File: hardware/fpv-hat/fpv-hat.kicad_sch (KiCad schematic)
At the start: 0 parts

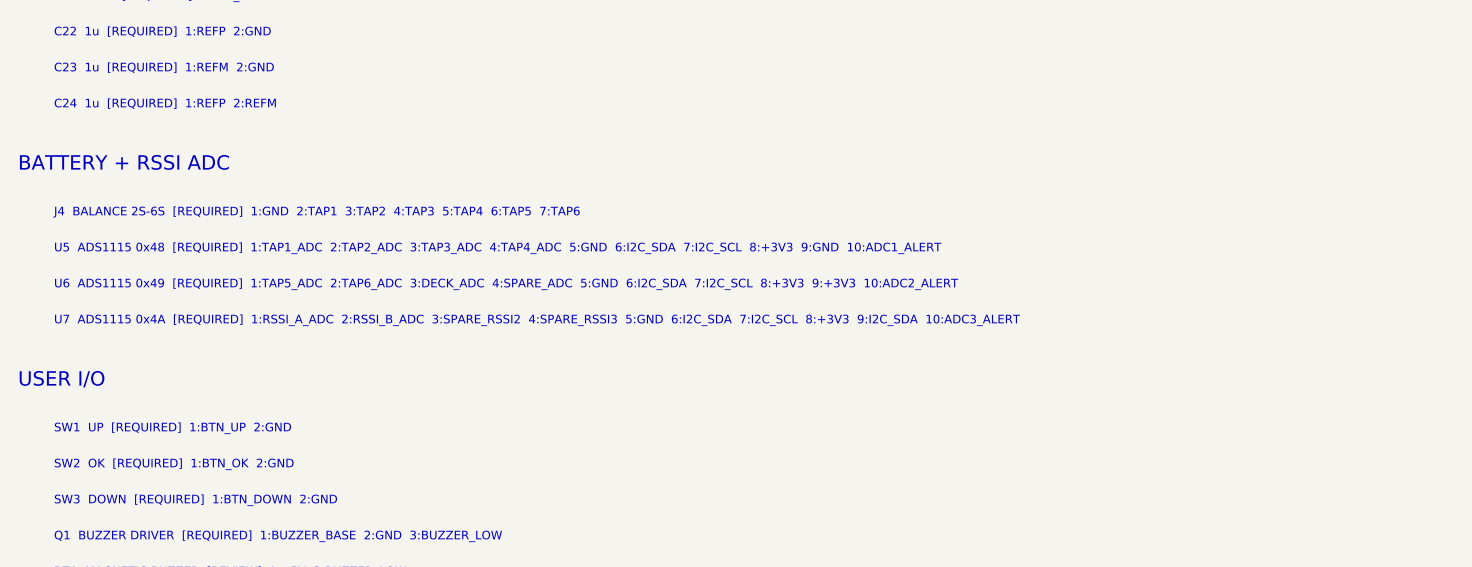
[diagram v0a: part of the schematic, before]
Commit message: fix(hw): correct ADS1115 pinout and decoupling
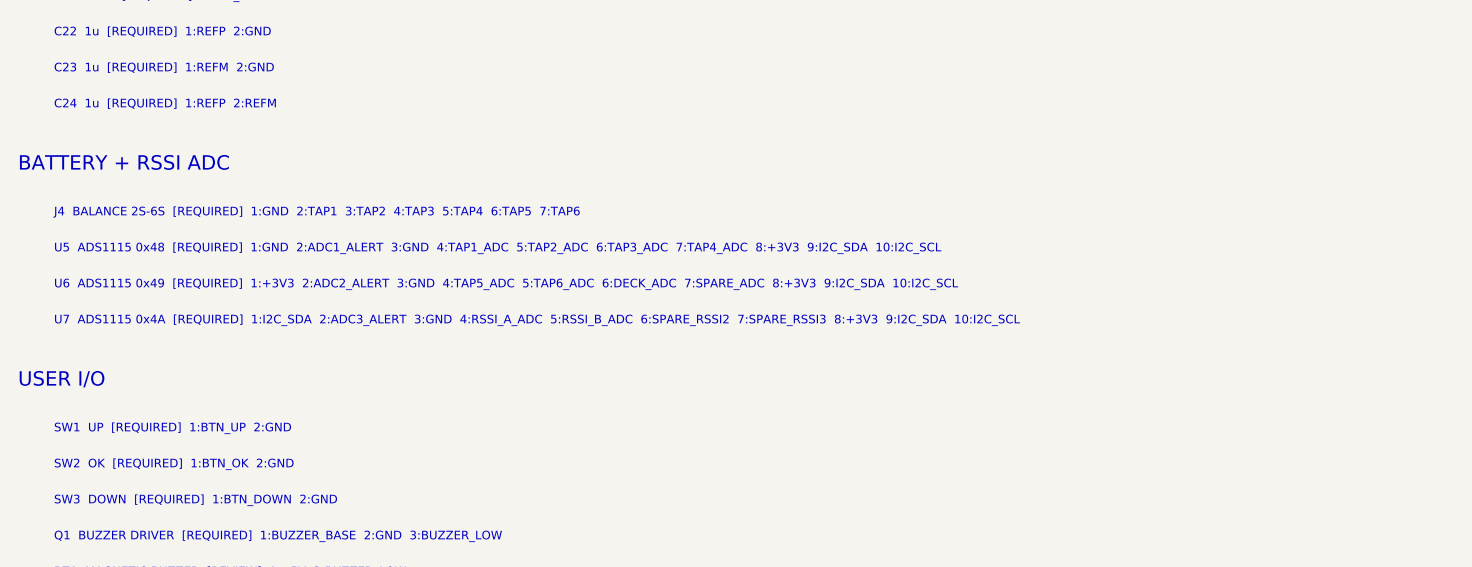
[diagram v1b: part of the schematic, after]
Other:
- note added: "U5 ADS1115 0x48 [REQUIRED] 1:GND 2:ADC1_ALERT 3:GND 4:TAP1_ADC 5:TAP2_ADC 6:TAP3_ADC 7:TAP4_ADC 8:+3V3 9:I2C_SDA 10:I2C_SCL"
- note added: "U6 ADS1115 0x49 [REQUIRED] 1:+3V3 2:ADC2_ALERT 3:GND 4:TAP5_ADC 5:TAP6_ADC 6:DECK_ADC 7:SPARE_ADC 8:+3V3 9:I2C_SDA 10:I2C_SCL"
- note added: "U7 ADS1115 0x4A [REQUIRED] 1:I2C_SDA 2:ADC3_ALERT 3:GND 4:RSSI_A_ADC 5:RSSI_B_ADC 6:SPARE_RSSI2 7:SPARE_RSSI3 8:+3V3 9:I2C_SDA 10:I2C_SCL"
- note removed: "U5 ADS1115 0x48 [REQUIRED] 1:TAP1_ADC 2:TAP2_ADC 3:TAP3_ADC 4:TAP4_ADC 5:GND 6:I2C_SDA 7:I2C_SCL 8:+3V3 9:GND 10:ADC1_ALERT"
- note removed: "U6 ADS1115 0x49 [REQUIRED] 1:TAP5_ADC 2:TAP6_ADC 3:DECK_ADC 4:SPARE_ADC 5:GND 6:I2C_SDA 7:I2C_SCL 8:+3V3 9:+3V3 10:ADC2_ALERT"
- note removed: "U7 ADS1115 0x4A [REQUIRED] 1:RSSI_A_ADC 2:RSSI_B_ADC 3:SPARE_RSSI2 4:SPARE_RSSI3 5:GND 6:I2C_SDA 7:I2C_SCL 8:+3V3 9:I2C_SDA 10:ADC3_ALERT"
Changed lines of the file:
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@@
     (effects (font (size 0.95 0.95)) (justify left bottom))
 )
-  (text "U5  ADS1115 0x48  [REQUIRED]  1:TAP1_ADC  2:TAP2_ADC  3:TAP3_ADC  4:TAP4_ADC  5:GND  6:I2C_SDA  7:I2C_SCL  8:+3V3  9:GND  10:ADC1_ALERT" (at 24 141 0)
+  (text "U5  ADS1115 0x48  [REQUIRED]  1:GND  2:ADC1_ALERT  3:GND  4:TAP1_ADC  5:TAP2_ADC  6:TAP3_ADC  7:TAP4_ADC  8:+3V3  9:I2C_SDA  10:I2C_SCL" (at 24 141 0)
     (effects (font (size 0.95 0.95)) (justify left bottom))
 )
-  (text "U6  ADS1115 0x49  [REQUIRED]  1:TAP5_ADC  2:TAP6_ADC  3:DECK_ADC  4:SPARE_ADC  5:GND  6:I2C_SDA  7:I2C_SCL  8:+3V3  9:+3V3  10:ADC2_ALERT" (at 24 145 0)
+  (text "U6  ADS1115 0x49  [REQUIRED]  1:+3V3  2:ADC2_ALERT  3:GND  4:TAP5_ADC  5:TAP6_ADC  6:DECK_ADC  7:SPARE_ADC  8:+3V3  9:I2C_SDA  10:I2C_SCL" (at 24 145 0)
     (effects (font (size 0.95 0.95)) (justify left bottom))
 )
-  (text "U7  ADS1115 0x4A  [REQUIRED]  1:RSSI_A_ADC  2:RSSI_B_ADC  3:SPARE_RSSI2  4:SPARE_RSSI3  5:GND  6:I2C_SDA  7:I2C_SCL  8:+3V3  9:I2C_SDA  10:ADC3_ALERT" (at 24 149 0)
+  (text "U7  ADS1115 0x4A  [REQUIRED]  1:I2C_SDA  2:ADC3_ALERT  3:GND  4:RSSI_A_ADC  5:RSSI_B_ADC  6:SPARE_RSSI2  7:SPARE_RSSI3  8:+3V3  9:I2C_SDA  10:I2C_SCL" (at 24 149 0)
     (effects (font (size 0.95 0.95)) (justify left bottom))
 )

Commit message: fix(hw): add verified decoder power networks
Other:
- note added: "CA1 100n 16V X7R [REQUIRED] 1:+3V3 2:GND"
- note added: "CA2 100n 16V X7R [REQUIRED] 1:+3V3 2:GND"
- note added: "CA3 100n 16V X7R [REQUIRED] 1:+3V3 2:GND"
- note added: "CD1 100n 16V X7R [REQUIRED] 1:+1V8A 2:GND"
- note added: "CD2 100n 16V X7R [REQUIRED] 1:+1V8A 2:GND"
- note added: "CD3 100n 16V X7R [REQUIRED] 1:+1V8D 2:GND"
- note added: "CD4 100n 16V X7R [REQUIRED] 1:+3V3 2:GND"
- note added: "CIN1 1u 10V X7R [REQUIRED] 1:+5V 2:GND"
- note added: "COUT1 1u 10V X7R [REQUIRED] 1:+1V8 2:GND"
- note added: "CY1 CRYSTAL LOAD TUNE [DNP] 1:XTAL1 2:GND"
- note added: "CY2 CRYSTAL LOAD TUNE [DNP] 1:XTAL2 2:GND"
- note added: "RY1 100k 1% [REQUIRED] 1:XTAL1 2:XTAL2"

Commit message: feat(hw): add dual RX5808 final-form HAT layout
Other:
- note added: "C1 100n 16V X7R [REQUIRED] 1:+3V3 2:GND"
- note added: "C2 100n 16V X7R [REQUIRED] 1:+3V3 2:GND"
- note added: "CRA1 100n 16V X7R [REQUIRED] 1:+5V_RX_A 2:GND"
- note added: "CRA2 10u 10V X7R [REQUIRED] 1:+5V_RX_A 2:GND"
- note added: "CRB1 100n 16V X7R [REQUIRED] 1:+5V_RX_B 2:GND"
- note added: "CRB2 10u 10V X7R [REQUIRED] 1:+5V_RX_B 2:GND"
- note added: "FRA 220R@100MHz 2A [REQUIRED] 1:+5V 2:+5V_RX_A"
- note added: "FRB 220R@100MHz 2A [REQUIRED] 1:+5V 2:+5V_RX_B"
- note added: "J1 WAVESHARE 40PIN [REQUIRED] 1:+5V 2:+3V3 3:+5V 4:I2C_SDA 5:GND 6:I2C_SCL 7:DVP_D0 8:VIDEO_SELECT_MCU 9:DVP_D1 11:DVP_D2 12:DVP_D3 14:DVP_D4 15:DVP_D5 16:DVP_D6 17:DVP_D7 18:+3V3 20:DVP_PCLK 22:DVP_HSYNC 24:DVP_VSYNC 26:GND 28:RX_DATA 30:RX_CLK 31:RX_LE_A 32:RX_LE_B 34:VIDEO_SELECT 35:TVP_RESETB 36:BTN_UP 37:BTN_OK 38:BTN_DOWN 39:BUZZER 40:GND"
- note added: "J3 SMA EDGE B [REQUIRED] 1:RF_B 2:GND"
- note added: "JP1 AUTO / MCU SELECT [REQUIRED] 1:RX_A_STRONGER 2:VIDEO_SELECT 3:VIDEO_SELECT_MCU"
- note added: "RXA RX5808 MODULE A [REQUIRED] 1:GND 2:RF_A 3:GND 4:RX_DATA 5:RX_LE_A 6:RX_CLK 7:GND 8:+5V_RX_A 9:RSSI_A 10:NC_AUDIO_A 11:VIDEO_A 12:GND"
- note added: "RXB RX5808 MODULE B [REQUIRED] 1:GND 2:RF_B 3:GND 4:RX_DATA 5:RX_LE_B 6:RX_CLK 7:GND 8:+5V_RX_B 9:RSSI_B 10:NC_AUDIO_B 11:VIDEO_B 12:GND"
- note added: "U1 RSSI COMPARATOR [REQUIRED] 1:RX_A_STRONGER 2:GND 3:RSSI_A_HYS 4:RSSI_B 5:+3V3"
- note added: "U2 VIDEO SWITCH [REQUIRED] 1:VIDEO_A 2:GND 3:VIDEO_B 4:VIDEO_SELECTED 5:+3V3 6:VIDEO_SELECT"
- note removed: "J1 WAVESHARE 40PIN [REQUIRED] 1:+5V 2:+3V3 3:+5V 4:I2C_SDA 5:GND 6:I2C_SCL 7:DVP_D0 9:DVP_D1 11:DVP_D2 12:DVP_D3 14:DVP_D4 15:DVP_D5 16:DVP_D6 17:DVP_D7 18:+3V3 20:DVP_PCLK 22:DVP_HSYNC 24:DVP_VSYNC 26:GND 28:RX_DATA 30:RX_CLK 31:RX_LE_A 32:RX_LE_B 34:ACTIVE_RX 35:TVP_RESETB 36:BTN_UP 37:BTN_OK 38:BTN_DOWN 39:BUZZER 40:GND"
- note removed: "J3 SMA EDGE B [DNP] 1:RF_B 2:GND"
- note removed: "RXA RX5808 MODULE A [REQUIRED] 1:GND 2:RF_A 3:GND 4:RX_DATA 5:RX_LE_A 6:RX_CLK 7:GND 8:+5V 9:RSSI_A 10:NC_AUDIO_A 11:VIDEO_A"
- note removed: "RXB RX5808 MODULE B [DNP] 1:GND 2:RF_B 3:GND 4:RX_DATA 5:RX_LE_B 6:RX_CLK 7:GND 8:+5V 9:RSSI_B 10:NC_AUDIO_B 11:VIDEO_B"
- note removed: "U1 RSSI COMPARATOR [REQUIRED] 1:ACTIVE_RX 2:GND 3:RSSI_A_HYS 4:RSSI_B 5:+3V3"
- note removed: "U2 VIDEO SWITCH [REQUIRED] 1:VIDEO_A 2:GND 3:VIDEO_B 4:VIDEO_SELECTED 5:+3V3 6:ACTIVE_RX"

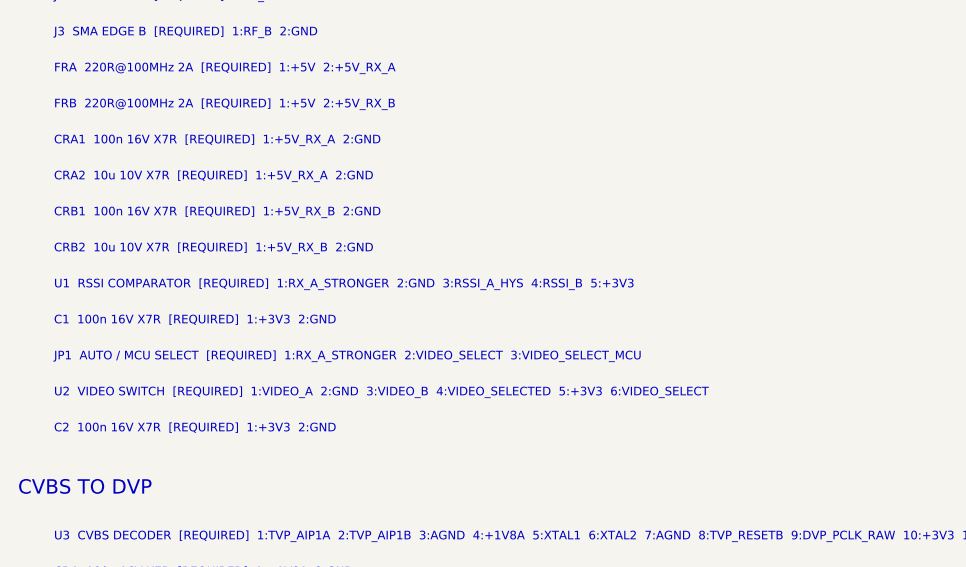
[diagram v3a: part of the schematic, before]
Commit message: fix(hw): correct LMV331 diversity pin mapping
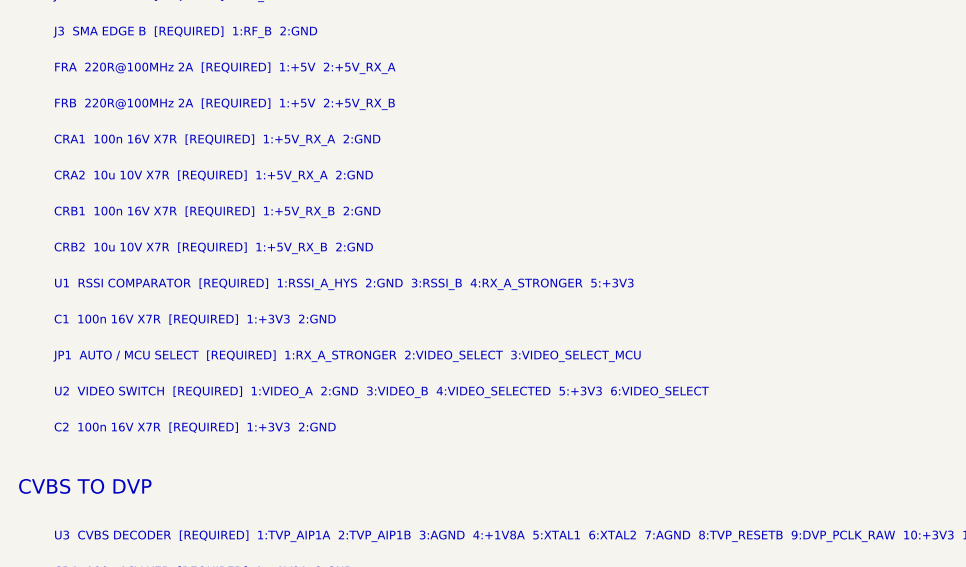
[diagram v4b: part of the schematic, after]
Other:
- note added: "U1 RSSI COMPARATOR [REQUIRED] 1:RSSI_A_HYS 2:GND 3:RSSI_B 4:RX_A_STRONGER 5:+3V3"
- note removed: "U1 RSSI COMPARATOR [REQUIRED] 1:RX_A_STRONGER 2:GND 3:RSSI_A_HYS 4:RSSI_B 5:+3V3"
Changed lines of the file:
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@@
     (effects (font (size 0.95 0.95)) (justify left bottom))
 )
-  (text "U1  RSSI COMPARATOR  [REQUIRED]  1:RX_A_STRONGER  2:GND  3:RSSI_A_HYS  4:RSSI_B  5:+3V3" (at 24 109 0)
+  (text "U1  RSSI COMPARATOR  [REQUIRED]  1:RSSI_A_HYS  2:GND  3:RSSI_B  4:RX_A_STRONGER  5:+3V3" (at 24 109 0)
     (effects (font (size 0.95 0.95)) (justify left bottom))
 )

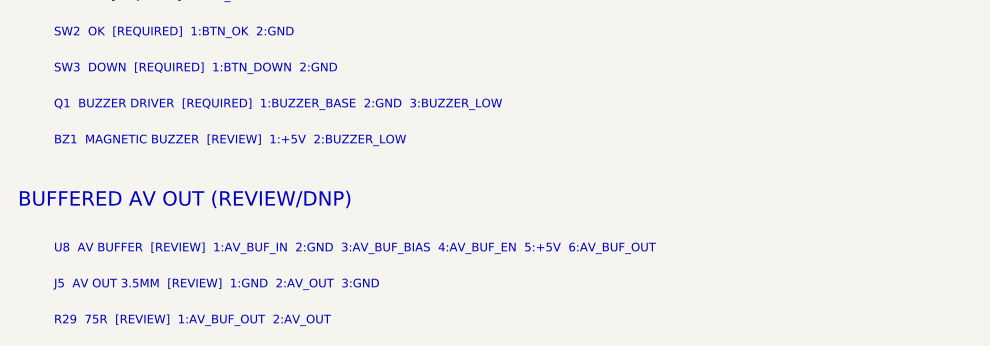
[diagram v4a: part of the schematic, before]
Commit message: fix(hw): complete verified buffered AV output
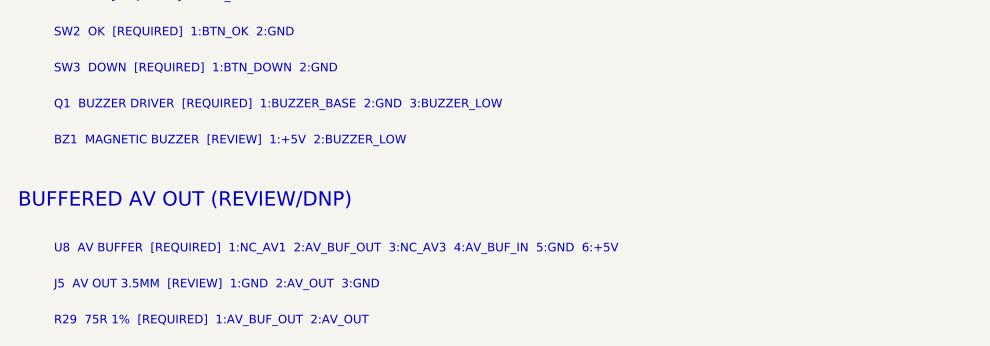
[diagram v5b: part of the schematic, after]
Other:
- note added: "R29 75R 1% [REQUIRED] 1:AV_BUF_OUT 2:AV_OUT"
- note added: "U8 AV BUFFER [REQUIRED] 1:NC_AV1 2:AV_BUF_OUT 3:NC_AV3 4:AV_BUF_IN 5:GND 6:+5V"
- note removed: "R29 75R [REVIEW] 1:AV_BUF_OUT 2:AV_OUT"
- note removed: "U8 AV BUFFER [REVIEW] 1:AV_BUF_IN 2:GND 3:AV_BUF_BIAS 4:AV_BUF_EN 5:+5V 6:AV_BUF_OUT"
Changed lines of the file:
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@@
     (effects (font (size 1.6 1.6)) (justify left bottom))
 )
-  (text "U8  AV BUFFER  [REVIEW]  1:AV_BUF_IN  2:GND  3:AV_BUF_BIAS  4:AV_BUF_EN  5:+5V  6:AV_BUF_OUT" (at 24 273 0)
+  (text "U8  AV BUFFER  [REQUIRED]  1:NC_AV1  2:AV_BUF_OUT  3:NC_AV3  4:AV_BUF_IN  5:GND  6:+5V" (at 24 273 0)
     (effects (font (size 0.95 0.95)) (justify left bottom))
 )
@@
     (effects (font (size 0.95 0.95)) (justify left bottom))
 )
-  (text "R29  75R  [REVIEW]  1:AV_BUF_OUT  2:AV_OUT" (at 24 281 0)
+  (text "R29  75R 1%  [REQUIRED]  1:AV_BUF_OUT  2:AV_OUT" (at 24 281 0)
     (effects (font (size 0.95 0.95)) (justify left bottom))
 )
